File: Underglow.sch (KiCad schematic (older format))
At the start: 10 parts

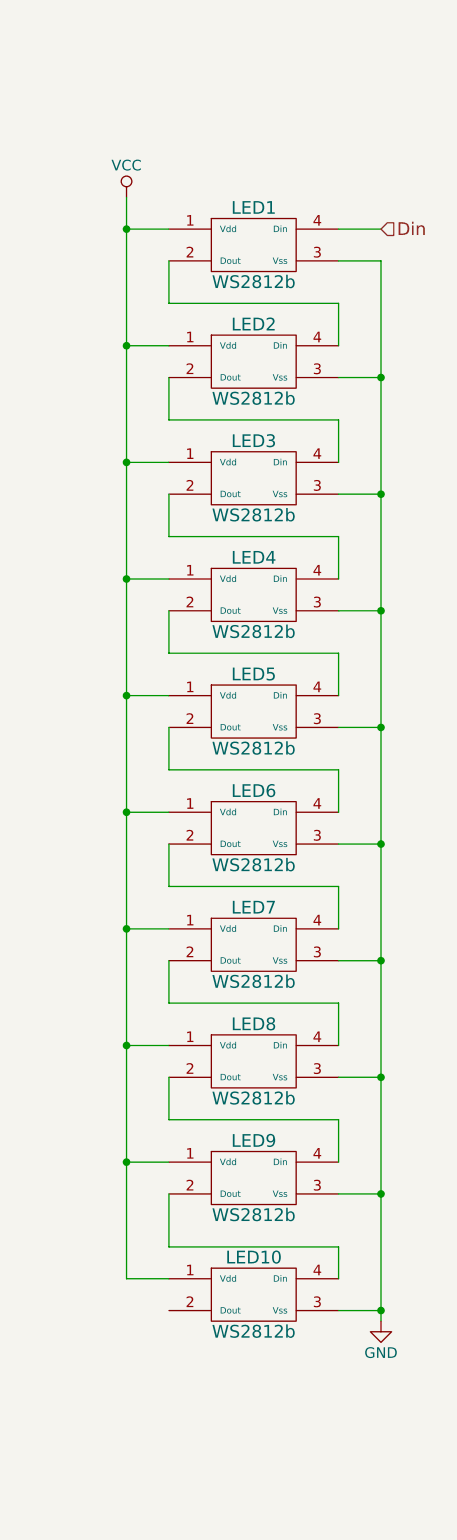
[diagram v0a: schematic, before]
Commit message: Added 0.1uF caps to LEDs
Added capacitors from Vcc to GND for WS2812s
Also changed some references
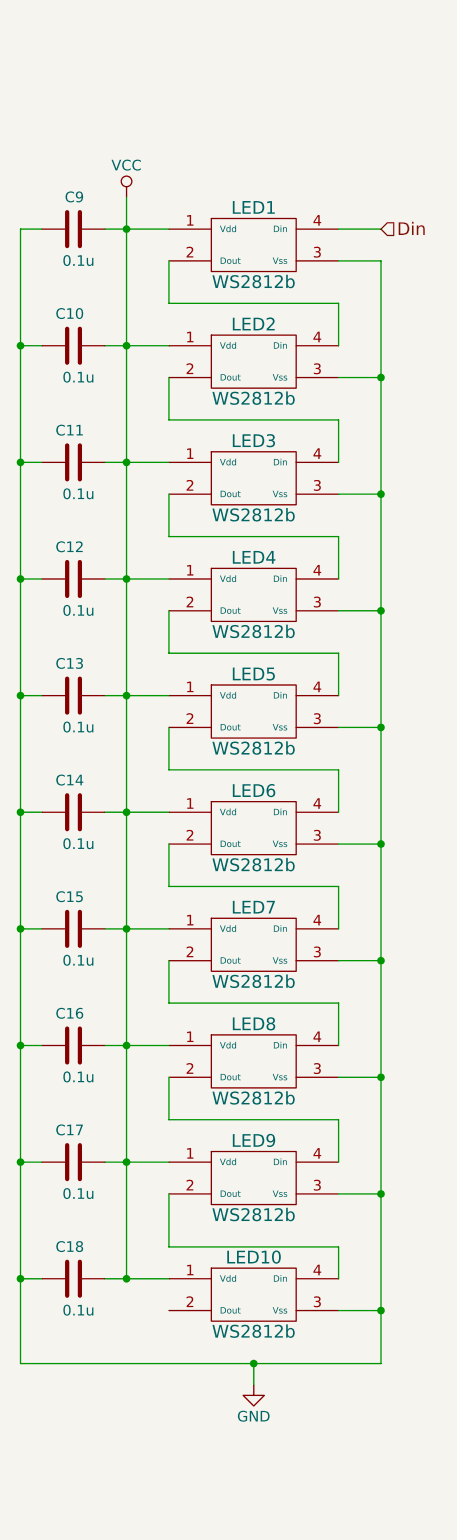
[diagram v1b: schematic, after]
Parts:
- added C10, C11, C12, C13, C14, C15, C16, C17, C18, C9: 0.1u, Capacitors_SMD:C_0805, symbol C
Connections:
- net GND: now also C10.1, C11.1, C12.1, C13.1, C14.1, C15.1, C16.1, C17.1, C18.1, C9.1
- net VCC: now also C10.2, C11.2, C12.2, C13.2, C14.2, C15.2, C16.2, C17.2, C18.2, C9.2
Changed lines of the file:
@@
 	2050 1400 2050 6500
 Wire Wire Line
-	2050 4300 2250 4300
-Wire Wire Line
-	2250 3750 2050 3750
+	1950 4300 2250 4300
+Wire Wire Line
+	1950 3750 2250 3750
 Connection ~ 2050 3750
 Wire Wire Line
-	2250 3200 2050 3200
+	1950 3200 2250 3200
 Connection ~ 2050 3200
 Wire Wire Line
-	2250 2650 2050 2650
+	1950 2650 2250 2650
 Connection ~ 2050 2650
 Wire Wire Line
-	2250 2100 2050 2100
+	1950 2100 2250 2100
 Connection ~ 2050 2100
 Wire Wire Line
-	2250 1550 2050 1550
+	1950 1550 2250 1550
 Connection ~ 2050 1550
 $Comp
 L GND #PWR027
 U 1 1 59158759
-P 3250 6700
-F 0 "#PWR027" H 3250 6450 50  0001 C CNN
-F 1 "GND" H 3250 6550 50  0000 C CNN
-F 2 "" H 3250 6700 50  0000 C CNN
-F 3 "" H 3250 6700 50  0000 C CNN
-	1    3250 6700
-	1    0    0    -1
-$EndComp
-Wire Wire Line
-	3250 1700 3250 6700
+P 2650 7000
+F 0 "#PWR027" H 2650 6750 50  0001 C CNN
+F 1 "GND" H 2650 6850 50  0000 C CNN
+F 2 "" H 2650 7000 50  0000 C CNN
+F 3 "" H 2650 7000 50  0000 C CNN
+	1    2650 7000
+	1    0    0    -1
+$EndComp
+Wire Wire Line
+	3250 6900 3250 1700
 Wire Wire Line
 	3250 1700 3050 1700
@@
 	3050 6350 3050 6500
 Wire Wire Line
-	2050 4850 2250 4850
+	1950 4850 2250 4850
 Connection ~ 2050 4300
 Wire Wire Line
-	2050 5400 2250 5400
+	1950 5400 2250 5400
 Connection ~ 2050 4850
 Wire Wire Line
-	2050 5950 2250 5950
+	1950 5950 2250 5950
 Connection ~ 2050 5400
 Wire Wire Line
-	2050 6500 2250 6500
+	1950 6500 2250 6500
 Connection ~ 2050 5950
 Text HLabel 3250 1550 2    60   Input ~ 0
@@
 Wire Wire Line
 	3250 1550 3050 1550
+$Comp
+L C C9
+U 1 1 591BC6E7
+P 1800 1550
+F 0 "C9" V 1950 1500 50  0000 L CNN
+F 1 "0.1u" V 1650 1450 50  0000 L CNN
+F 2 "Capacitors_SMD:C_0805" H 1838 1400 50  0001 C CNN
+F 3 "" H 1800 1550 50  0000 C CNN
+	1    1800 1550
+	0    -1   -1   0
+$EndComp
+$Comp
+L C C10
+U 1 1 591BCE61
+P 1800 2100
+F 0 "C10" V 1950 2050 50  0000 L CNN
+F 1 "0.1u" V 1650 2000 50  0000 L CNN
+F 2 "Capacitors_SMD:C_0805" H 1838 1950 50  0001 C CNN
+F 3 "" H 1800 2100 50  0000 C CNN
+	1    1800 2100
+	0    -1   -1   0
+$EndComp
+$Comp
+L C C11
+U 1 1 591BCEA7
+P 1800 2650
+F 0 "C11" V 1950 2600 50  0000 L CNN
+F 1 "0.1u" V 1650 2550 50  0000 L CNN
+F 2 "Capacitors_SMD:C_0805" H 1838 2500 50  0001 C CNN
+F 3 "" H 1800 2650 50  0000 C CNN
+	1    1800 2650
+	0    -1   -1   0
+$EndComp
+$Comp
+L C C12
+U 1 1 591BCF98
+P 1800 3200
+F 0 "C12" V 1950 3150 50  0000 L CNN
+F 1 "0.1u" V 1650 3100 50  0000 L CNN
+F 2 "Capacitors_SMD:C_0805" H 1838 3050 50  0001 C CNN
+F 3 "" H 1800 3200 50  0000 C CNN
+	1    1800 3200
+	0    -1   -1   0
+$EndComp
+$Comp
+L C C13
+U 1 1 591BCFE8
+P 1800 3750
+F 0 "C13" V 1950 3700 50  0000 L CNN
+F 1 "0.1u" V 1650 3650 50  0000 L CNN
+F 2 "Capacitors_SMD:C_0805" H 1838 3600 50  0001 C CNN
+F 3 "" H 1800 3750 50  0000 C CNN
+	1    1800 3750
+	0    -1   -1   0
+$EndComp
+$Comp
+L C C14
+U 1 1 591BD037
+P 1800 4300
+F 0 "C14" V 1950 4250 50  0000 L CNN
+F 1 "0.1u" V 1650 4200 50  0000 L CNN
+F 2 "Capacitors_SMD:C_0805" H 1838 4150 50  0001 C CNN
+F 3 "" H 1800 4300 50  0000 C CNN
+	1    1800 4300
+	0    -1   -1   0
+$EndComp
+$Comp
+L C C15
+U 1 1 591BD165
+P 1800 4850
+F 0 "C15" V 1950 4800 50  0000 L CNN
+F 1 "0.1u" V 1650 4750 50  0000 L CNN
+F 2 "Capacitors_SMD:C_0805" H 1838 4700 50  0001 C CNN
+F 3 "" H 1800 4850 50  0000 C CNN
+	1    1800 4850
+	0    -1   -1   0
+$EndComp
+$Comp
+L C C16
+U 1 1 591BD1BE
+P 1800 5400
+F 0 "C16" V 1950 5350 50  0000 L CNN
+F 1 "0.1u" V 1650 5300 50  0000 L CNN
+F 2 "Capacitors_SMD:C_0805" H 1838 5250 50  0001 C CNN
+F 3 "" H 1800 5400 50  0000 C CNN
+	1    1800 5400
+	0    -1   -1   0
+$EndComp
+$Comp
+L C C17
+U 1 1 591BD3D8
+P 1800 5950
+F 0 "C17" V 1950 5900 50  0000 L CNN
+F 1 "0.1u" V 1650 5850 50  0000 L CNN
+F 2 "Capacitors_SMD:C_0805" H 1838 5800 50  0001 C CNN
+F 3 "" H 1800 5950 50  0000 C CNN
+	1    1800 5950
+	0    -1   -1   0
+$EndComp
+$Comp
+L C C18
+U 1 1 591BD433
+P 1800 6500
+F 0 "C18" V 1950 6450 50  0000 L CNN
+F 1 "0.1u" V 1650 6400 50  0000 L CNN
+F 2 "Capacitors_SMD:C_0805" H 1838 6350 50  0001 C CNN
+F 3 "" H 1800 6500 50  0000 C CNN
+	1    1800 6500
+	0    -1   -1   0
+$EndComp
+Connection ~ 2050 6500
+Wire Wire Line
+	1650 1550 1550 1550
+Wire Wire Line
+	1550 1550 1550 6900
+Wire Wire Line
+	1650 6500 1550 6500
+Connection ~ 1550 6500
+Wire Wire Line
+	1650 5950 1550 5950
+Connection ~ 1550 5950
+Wire Wire Line
+	1650 5400 1550 5400
+Connection ~ 1550 5400
+Wire Wire Line
+	1650 4850 1550 4850
+Connection ~ 1550 4850
+Wire Wire Line
+	1650 4300 1550 4300
+Connection ~ 1550 4300
+Wire Wire Line
+	1650 3750 1550 3750
+Connection ~ 1550 3750
+Wire Wire Line
+	1650 3200 1550 3200
+Connection ~ 1550 3200
+Wire Wire Line
+	1650 2650 1550 2650
+Connection ~ 1550 2650
+Wire Wire Line
+	1650 2100 1550 2100
+Connection ~ 1550 2100
+Wire Wire Line
+	2650 7000 2650 6900
+Wire Wire Line
+	1550 6900 3250 6900
+Connection ~ 2650 6900
 $EndSCHEMATC

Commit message: Connected most of the components on the board
TODO:
Replace P1 with 1x6 header for SPI, Vcc, GND
Add test pads
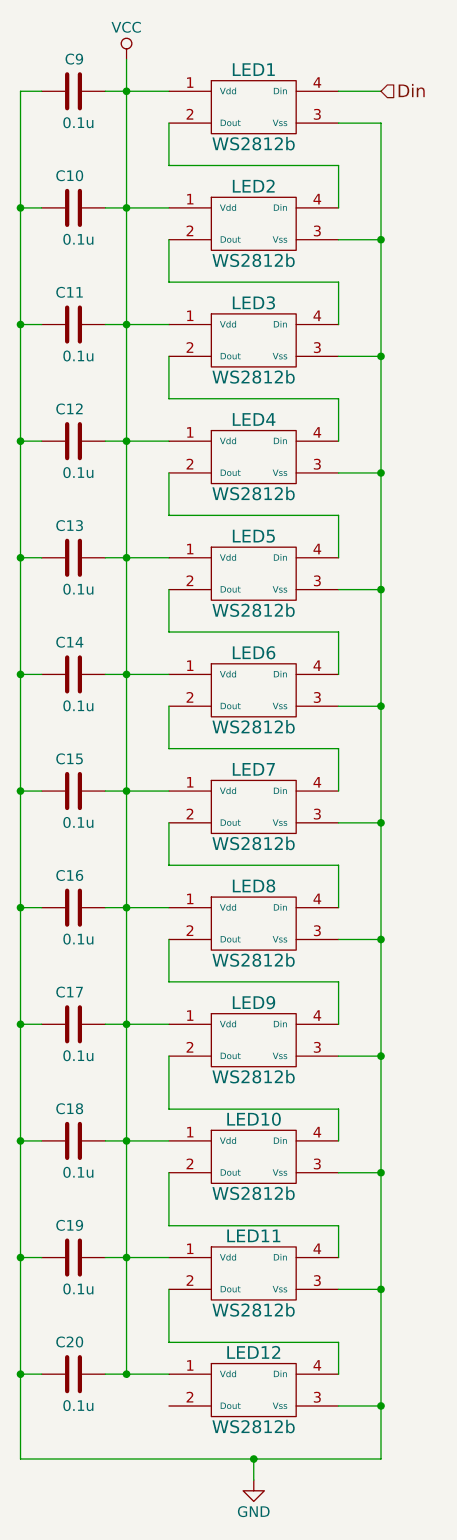
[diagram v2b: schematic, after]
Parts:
- added C19, C20: 0.1u, Capacitors_SMD:C_0805, symbol C
- added LED11, LED12: WS2812b, LEDs:LED_WS2812B-PLCC4, symbol WS2812b
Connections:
- net GND: now also C19.1, C20.1, LED11.3 (Vss), LED12.3 (Vss)
- net VCC: now also C19.2, C20.2, LED11.1 (Vdd), LED12.1 (Vdd)
- net at LED10.2 (Dout): now also LED11.4 (Din)
- new net: LED11.2 (Dout), LED12.4 (Din)
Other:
- moved on the sheet: C10, C11, C12, C13, C14, C15, C16, C17, C18, C9, LED1, LED10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
